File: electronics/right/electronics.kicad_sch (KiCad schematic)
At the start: 85 parts, among them J1 USB_C_Receptacle_USB2.0, J2 Battery Connector, SW1 SW_Reset, U1 Choc v1 Socket, U10 Choc v1 Socket, U11 Choc v1 Socket, U12 Choc v1 Socket, U13 Choc v1 Socket, U14 Choc v1 Socket, U15 Choc v1 Socket, U16 Choc v1 Socket, U17 Choc v1 Socket, U18 Choc v1 Socket, U19 Choc v1 Socket, U2 Choc v1 Socket, U20 Choc v1 Socket, U21 Choc v1 Socket, U22 nRF52840, U23 ESDR0502NMUTAG, U24 BQ24075RGT, U3 Choc v1 Socket, U4 Choc v1 Socket, U5 Choc v1 Socket, U6 Choc v1 Socket, U7 Choc v1 Socket, U8 Choc v1 Socket, U9 Choc v1 Socket, Y1 32.768 kHz, Y2 32MHz

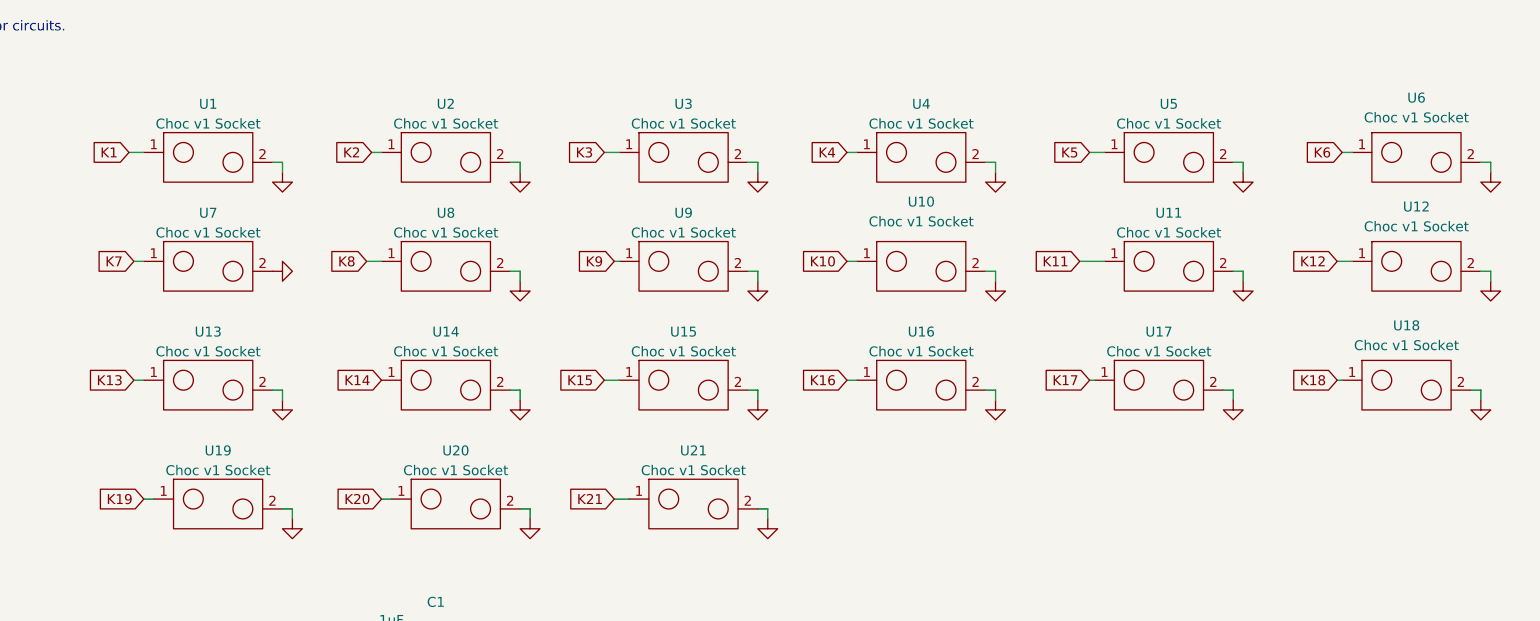
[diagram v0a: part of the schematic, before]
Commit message: Component metadata updates:
* Use official footprints for 0402 caps and resistors.
* Use correct JLC and LCSC part numbers for the choc switches.
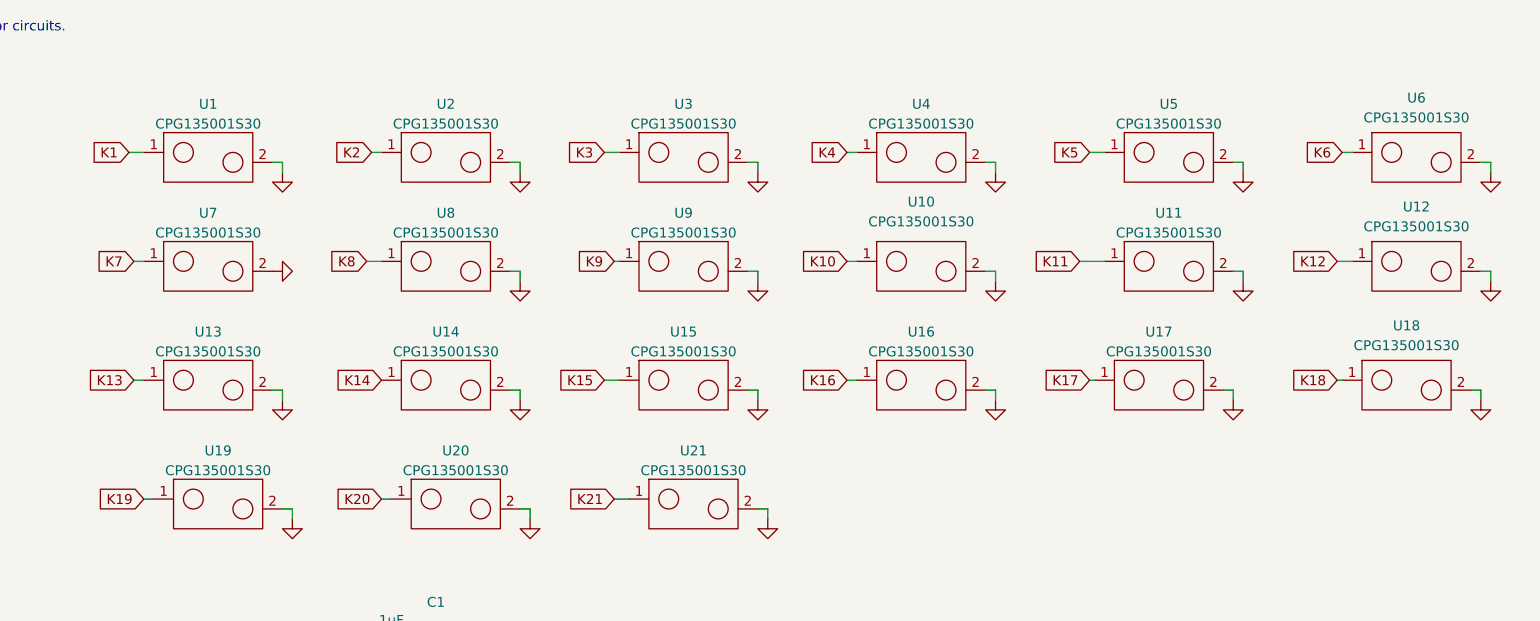
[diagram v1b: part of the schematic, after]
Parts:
- C1, C10, C11, C12, C13, C14, C15, C16, C17, C18, C19, C2, C20, C21, C22, C23, C24, C25, C26, C3, C4, C5, C6, C7, C8, C9: footprint lib:C_0402_1005Metric -> Capacitor_SMD:C_0402_1005Metric
- R1, R10, R11, R12, R2, R3, R4, R5, R6, R7, R8, R9: footprint lib:R_0402_1005Metric -> Resistor_SMD:R_0402_1005Metric
- U1, U10, U11, U12, U13, U14, U15, U16, U17, U18, U19, U2, U20, U21, U3, U4, U5, U6, U7, U8, U9: value Choc v1 Socket -> CPG135001S30; JLC Part C2803348 -> C5333465; LCSC Part C2803348 -> C5333465

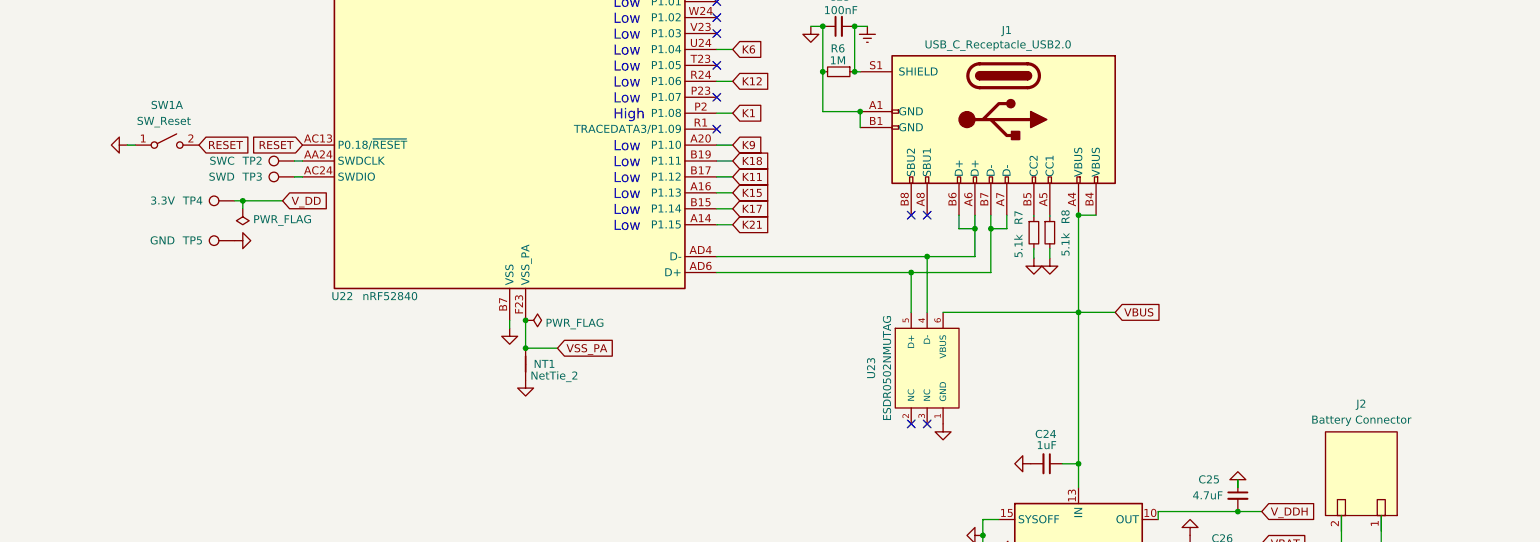
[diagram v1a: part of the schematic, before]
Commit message: Value update for battery connector and reset switch.
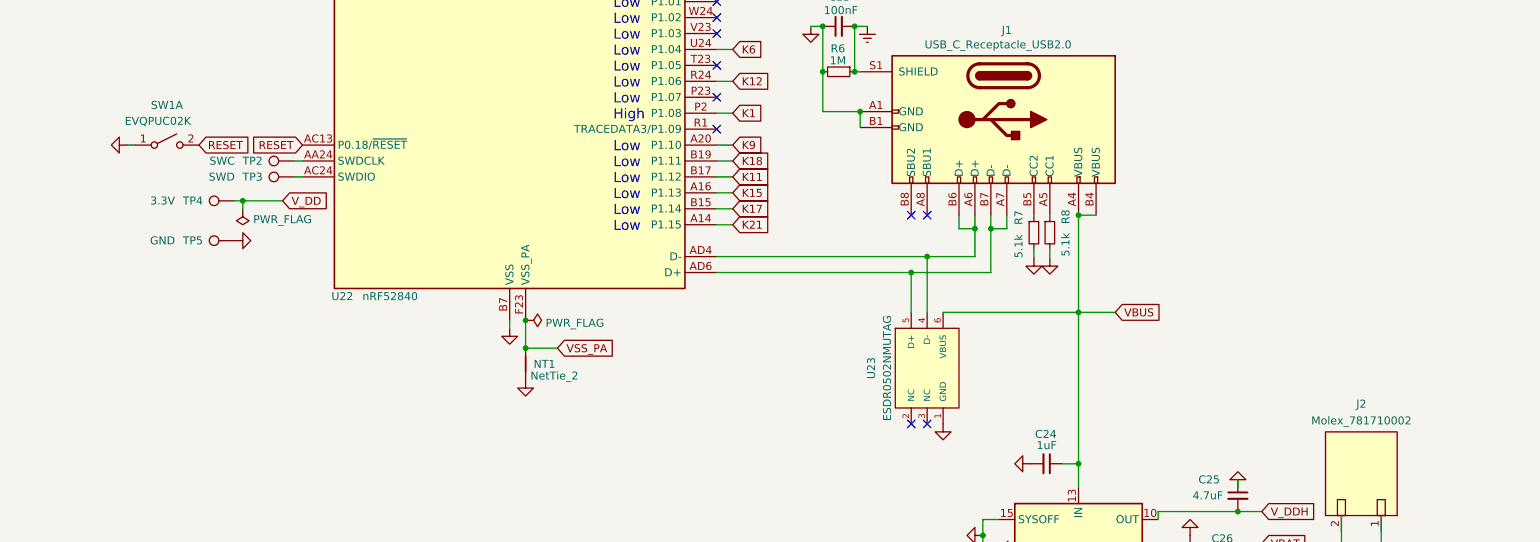
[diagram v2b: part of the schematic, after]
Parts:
- J2: value Battery Connector -> Molex_781710002; symbol Molex_Pico-EZmate_78171-0002_1x02-1MP_P1.20mm_Vertical:Battery Connector -> Molex_Pico-EZmate_78171-0002_1x02-1MP_P1.20mm_Vertical:Molex_781710002
- SW1: value SW_Reset -> EVQPUC02K
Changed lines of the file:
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@@
       (effects (font (size 1.27 1.27)) (justify right))
     )
-    (property "Value" "SW_Reset" (at 60.96 252.73 0)
+    (property "Value" "EVQPUC02K" (at 60.96 252.73 0)
       (effects (font (size 1.27 1.27)) (justify right))
     )
@@
       (effects (font (size 1.27 1.27)) hide)
     )
-    (property "Datasheet" "~" (at 57.15 256.54 0)
+    (property "Datasheet" "" (at 57.15 256.54 0)
       (effects (font (size 1.27 1.27)) hide)
     )
@@
     )
   )
-  (symbol (lib_id "Molex_Pico-EZmate_78171-0002_1x02-1MP_P1.20mm_Vertical:Battery Connector") (at 247.523 308.61 180) (unit 1)
+  (symbol (lib_id "Molex_Pico-EZmate_78171-0002_1x02-1MP_P1.20mm_Vertical:Molex_781710002") (at 247.523 308.61 180) (unit 1)
     (in_bom yes) (on_board yes) (dnp no)
     (property "Reference" "J2" (at 247.523 297.815 0)
       (effects (font (size 1.27 1.27)))
     )
-    (property "Value" "Battery Connector" (at 247.523 300.355 0)
+    (property "Value" "Molex_781710002" (at 247.523 300.482 0)
       (effects (font (size 1.27 1.27)))
     )
@@
       (effects (font (size 1.27 1.27)) hide)
     )
-    (property "Manufacturer Part" "Molex_Pico-EZmate_78171-0002" (at 247.523 294.64 0)
+    (property "Manufacturer Part" "Molex_Pico-EZmate_78171-0002" (at 246.888 291.465 0)
       (effects (font (size 1.27 1.27)) hide)
     )
-    (property "LCSC Part" "C505023" (at 247.523 308.61 0)
+    (property "LCSC Part" "C505023" (at 248.158 294.64 0)
       (effects (font (size 1.27 1.27)) hide)
     )
-    (property "JLC Part" "C505023" (at 247.523 308.61 0)
+    (property "JLC Part" "C505023" (at 248.158 294.64 0)
       (effects (font (size 1.27 1.27)) hide)
     )

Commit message: BOM value updates:
USB C Receptable
Molex connector.
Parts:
- J1: LCSC Part (none) -> C2988367; Manufacturer Part (none) -> GT-USB-9014C
- J2: Manufacturer Part Molex_Pico-EZmate_78171-0002 -> 781710002
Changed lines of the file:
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@@
+      (effects (font (size 1.27 1.27)) hide)
+    )
+    (property "LCSC Part" "C2988367" (at 190.5 252.476 90)
+      (effects (font (size 1.27 1.27)) hide)
+    )
+    (property "Manufacturer Part" "GT-USB-9014C" (at 190.5 252.476 90)
       (effects (font (size 1.27 1.27)) hide)
     )
@@
       (effects (font (size 1.27 1.27)) hide)
     )
-    (property "Manufacturer Part" "Molex_Pico-EZmate_78171-0002" (at 246.888 291.465 0)
-      (effects (font (size 1.27 1.27)) hide)
-    )
+    (property "Manufacturer Part" "781710002" (at 246.888 291.465 0)
+      (effects (font (size 1.27 1.27)) hide)
+    )

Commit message: Add JLC Part number to LEDs
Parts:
- D1: JLC Part (none) -> C605447
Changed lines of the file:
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@@
+      (effects (font (size 1.27 1.27)) hide)
+    )
+    (property "JLC Part" "C605447" (at 187.325 187.96 0)
       (effects (font (size 1.27 1.27)) hide)
     )

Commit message: Use official symbol for charging IC.
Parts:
- U24: footprint lib:VQFN-16-1EP_3x3mm_P0.5mm_EP1.6x1.6mm -> Package_DFN_QFN:VQFN-16-1EP_3x3mm_P0.5mm_EP1.6x1.6mm; symbol BQ24075RGT:BQ24075RGT -> Battery_Management:BQ24075RGT
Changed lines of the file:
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@@
     )
   )
-  (symbol (lib_id "BQ24075RGT:BQ24075RGT") (at 202.438 326.39 0) (unit 1)
+  (symbol (lib_id "Battery_Management:BQ24075RGT") (at 202.438 326.39 0) (unit 1)
     (in_bom yes) (on_board yes) (dnp no)
     (property "Reference" "U24" (at 200.533 346.075 0)
@@
       (effects (font (size 1.27 1.27)) (justify left))
     )
-    (property "Footprint" "lib:VQFN-16-1EP_3x3mm_P0.5mm_EP1.6x1.6mm" (at 210.058 340.36 0)
+    (property "Footprint" "Package_DFN_QFN:VQFN-16-1EP_3x3mm_P0.5mm_EP1.6x1.6mm" (at 210.058 340.36 0)
       (effects (font (size 1.27 1.27)) (justify left) hide)
     )

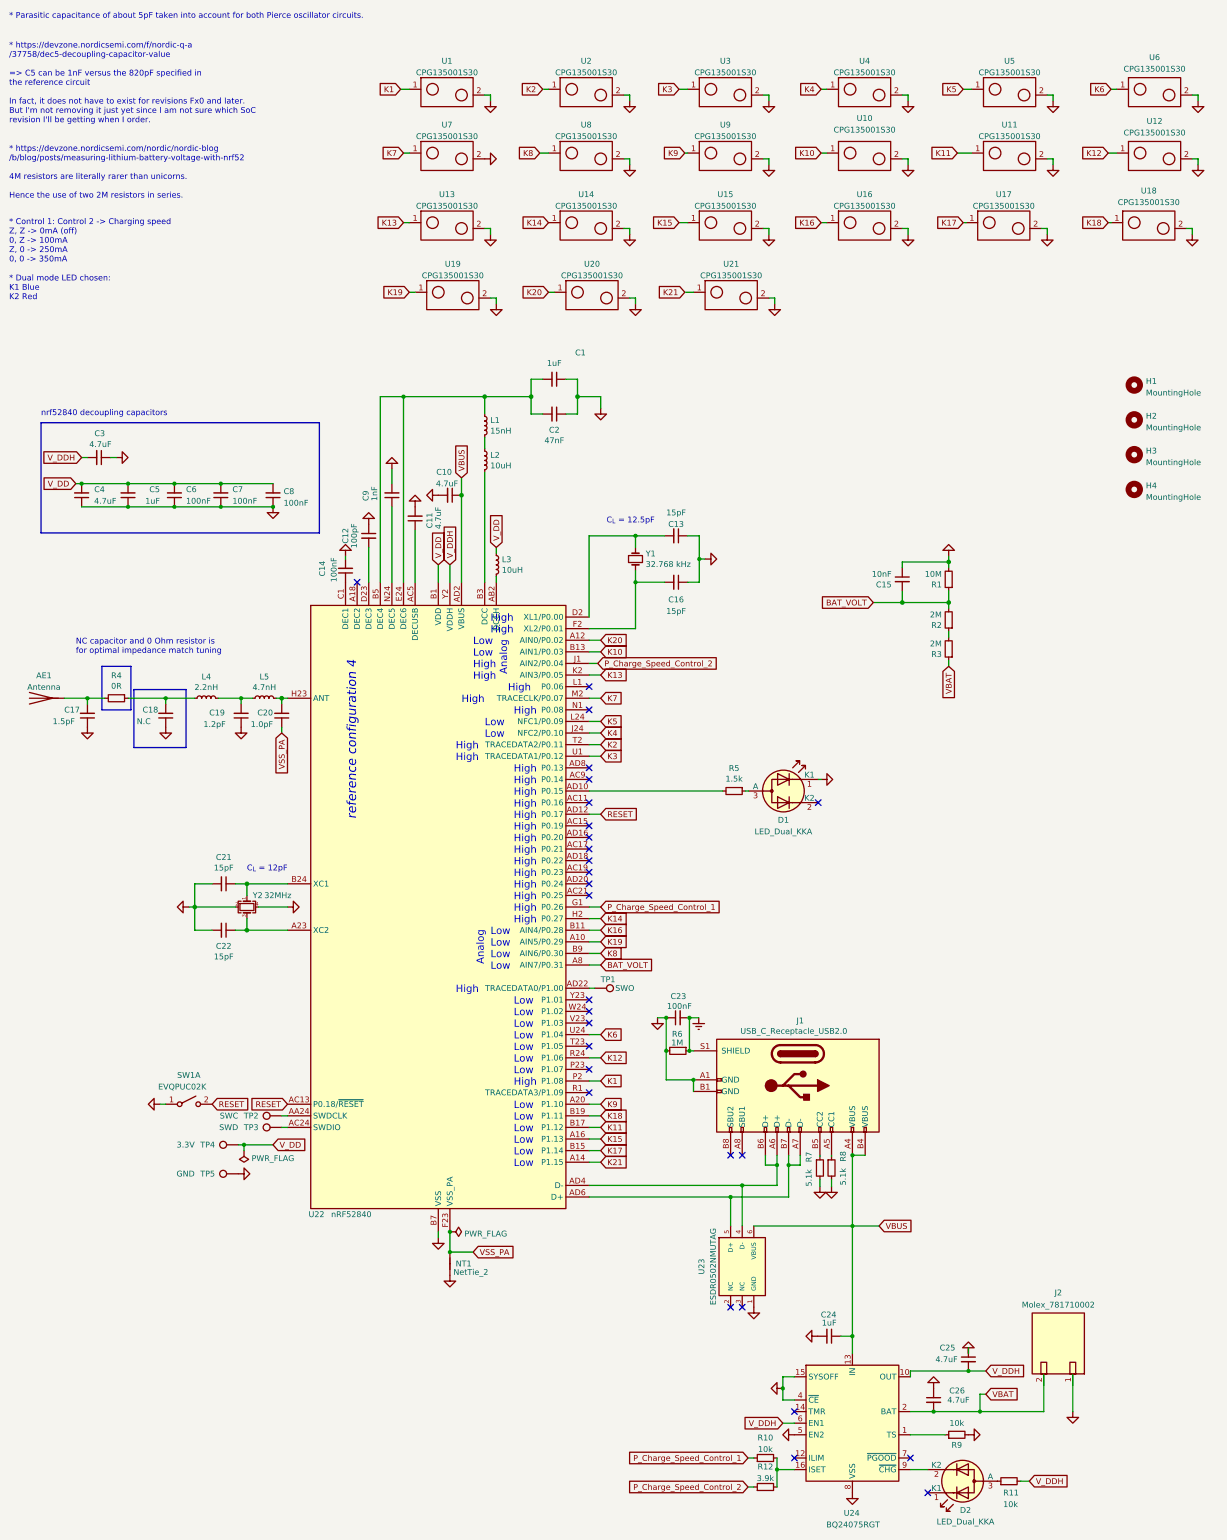
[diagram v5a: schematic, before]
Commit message: electronics/right: Fix schema and PCB references parity.
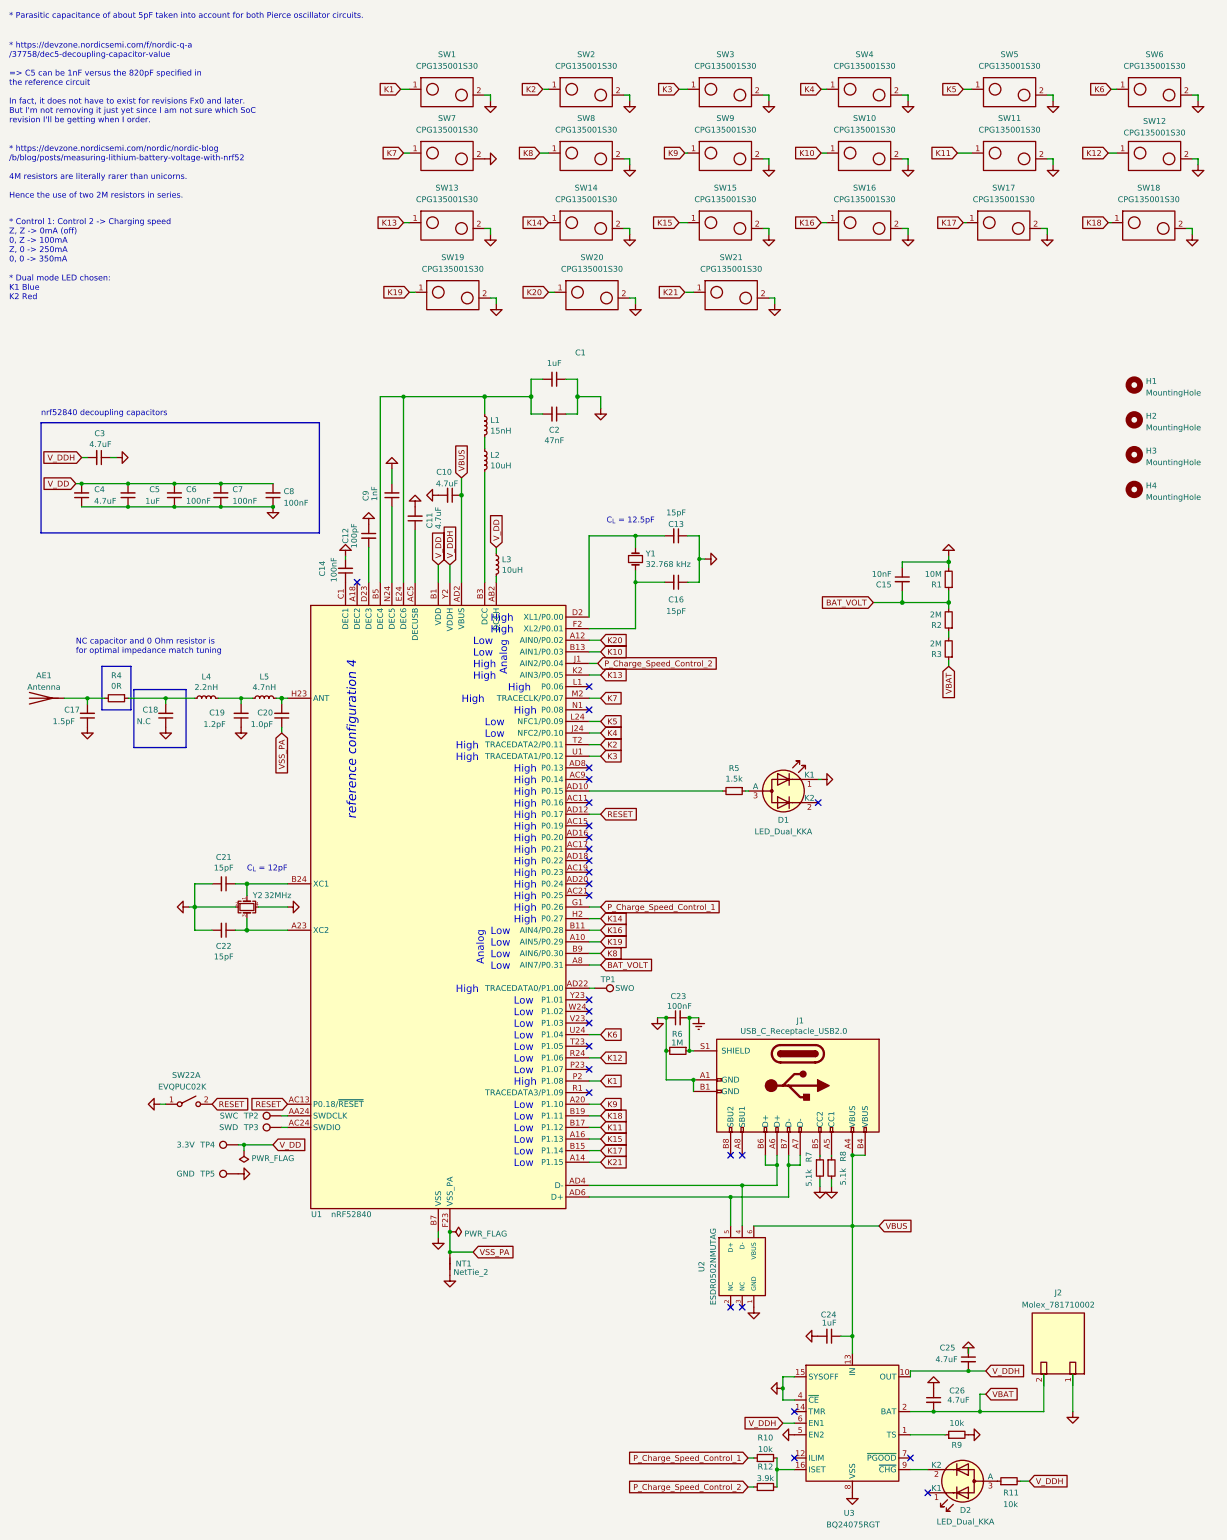
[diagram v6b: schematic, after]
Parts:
- renumbered U1 to SW1, U10 to SW10, U11 to SW11, U12 to SW12, U13 to SW13, U14 to SW14, U15 to SW15, U16 to SW16, U17 to SW17, U18 to SW18, U19 to SW19, U2 to SW2, U20 to SW20, U21 to SW21, SW1 to SW22, U3 to SW3, U4 to SW4, U5 to SW5, U6 to SW6, U7 to SW7, U8 to SW8, U9 to SW9, U22 to U1, U23 to U2, U24 to U3

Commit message: Make sure left and right halves produce the same BOM.
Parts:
- renumbered C8 to C10, C16 to C15, C15 to C16, C9 to C4, C10 to C5, C4 to C6, C5 to C7, C6 to C8, C7 to C9, R3 to R1, R1 to R3
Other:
- moved on the sheet: C10, C16, C3, C6, C7, C8, C9, R1, R2, R3
